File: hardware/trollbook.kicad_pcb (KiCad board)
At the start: 2 copper layers, 100 x 100 mm, 92 parts, among them P1 VGA, P10 CONN_1, P2 LCD, P3 SPI, P4 CONN_12, P5 CONN_2, P6 CONN_2, P7 CONN_2, P8 CONN_4, P9 CONN_2, U1 XC95288-208, U10 74LS574, U11 74LS574, U12 HY57V561620, U13 HY57V561620, U15 74HC4002, U16 ADA4851-4, U19 74HC139, U2 MC68030, U20 74HC10, U3 MC68882, U4 IDT71V416, U5 TLC7524, U6 74LS574, U7 39F040, U8 TLC7524, U9 74LS574, Y1 50 MHz, Y2 12.288 MHz

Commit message: fixed some erc/drc violations
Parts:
- added P11: CONN_2, PIN_ARRAY_2X1, F.Cu at (142.8, 153.7)
- P2: value LCD -> LCD_CONN
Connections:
- P2 pad GND: (no net) -> GND
- U1 pad 44: (no net) -> /EXTINT
- U15 pad 10: (no net) -> 3V3
- U15 pad 11: (no net) -> 3V3
- U15 pad 12: (no net) -> 3V3
- U15 pad 9: (no net) -> 3V3
- U19 pad 1: (no net) -> 3V3
- U19 pad 2: (no net) -> 3V3
- U19 pad 3: (no net) -> 3V3
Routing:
- net /EXTINT: track 0.00 -> 39.9 mm, vias 0 -> 4
- net 3V3: track 688.5 -> 704.6 mm
- net (no net): track 0.00 -> 4.55 mm, vias 0 -> 2
- net /CLK12: track 43.0 -> 42.2 mm
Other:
- board text added: "CPU"
- board text added: "DAC"
- board text added: "DRAM"
- board text added: "FPU"
- board text added: "GLUE"
- board text added: "ROM"
- board text added: "SRAM"

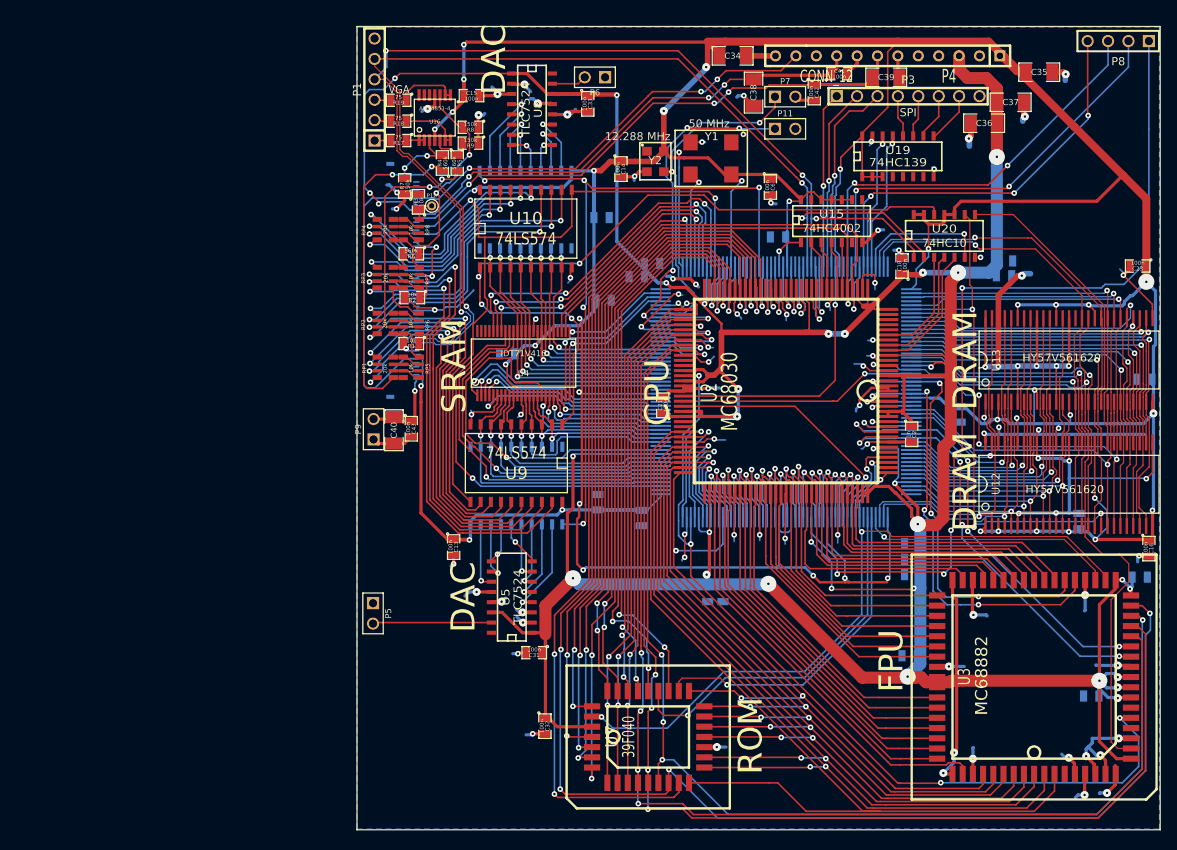
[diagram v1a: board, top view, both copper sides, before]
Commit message: ground plane stitching
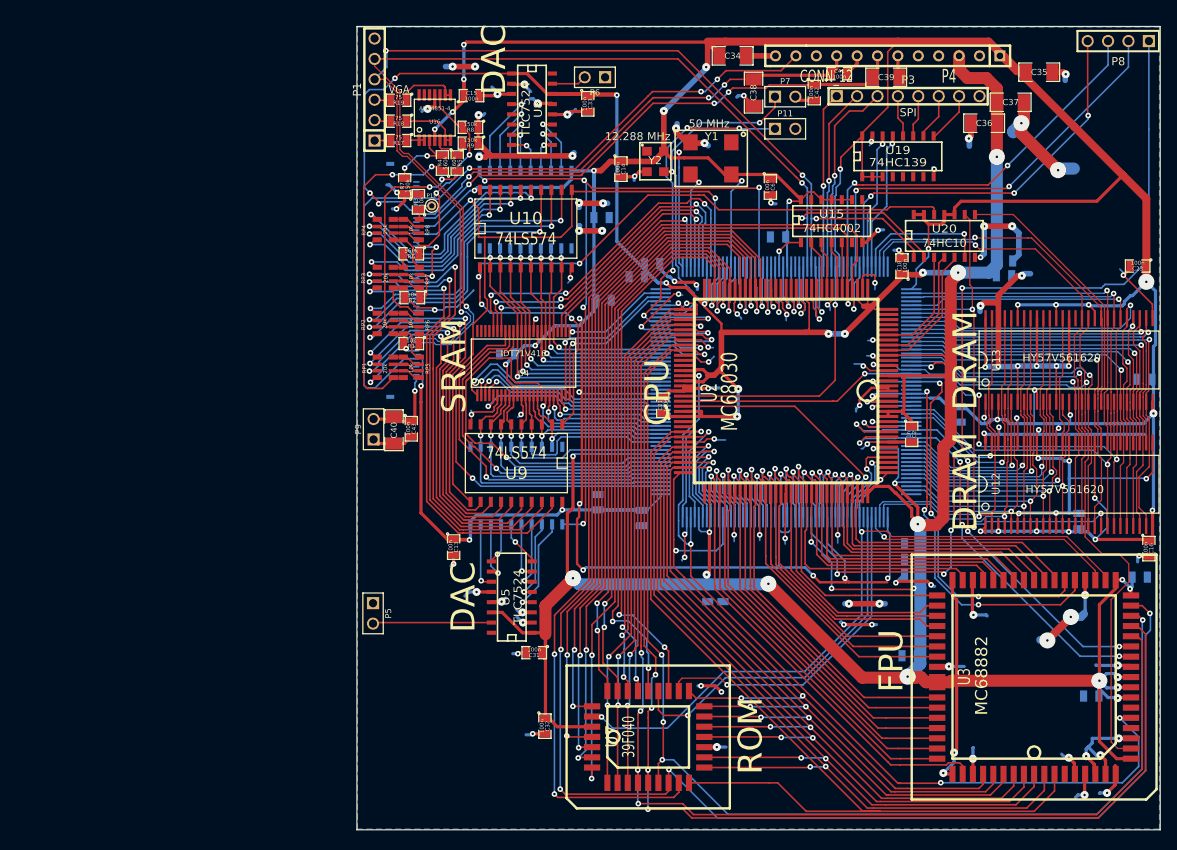
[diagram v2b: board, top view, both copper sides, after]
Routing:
- net GND: track 418.6 -> 484.4 mm, vias 85 -> 98
- net (no net): track 4.55 -> 24.7 mm, vias 2 -> 12
- net /DSACK1: track 54.8 -> 53.8 mm
- net /DSACK0: track 55.0 -> 53.9 mm
- net /D21: track 38.7 -> 39.4 mm

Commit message: arne
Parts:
- added R10: 10k, SM0805, F.Cu at (181.7, 146.7)
- added R11: 10k, SM0805, F.Cu at (183.8, 146.7)
- added R12: 10k, SM0805, F.Cu at (186.0, 146.7)
- added R13: 10k, SM0805, F.Cu at (188.2, 146.7)
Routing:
- net 3V3: track 704.6 -> 719.2 mm
- net N-0000055: track 49.9 -> 53.4 mm
- net N-0000056: track 51.6 -> 54.9 mm
- net N-0000057: track 53.0 -> 56.2 mm
- net N-0000058: track 110.4 -> 113.4 mm

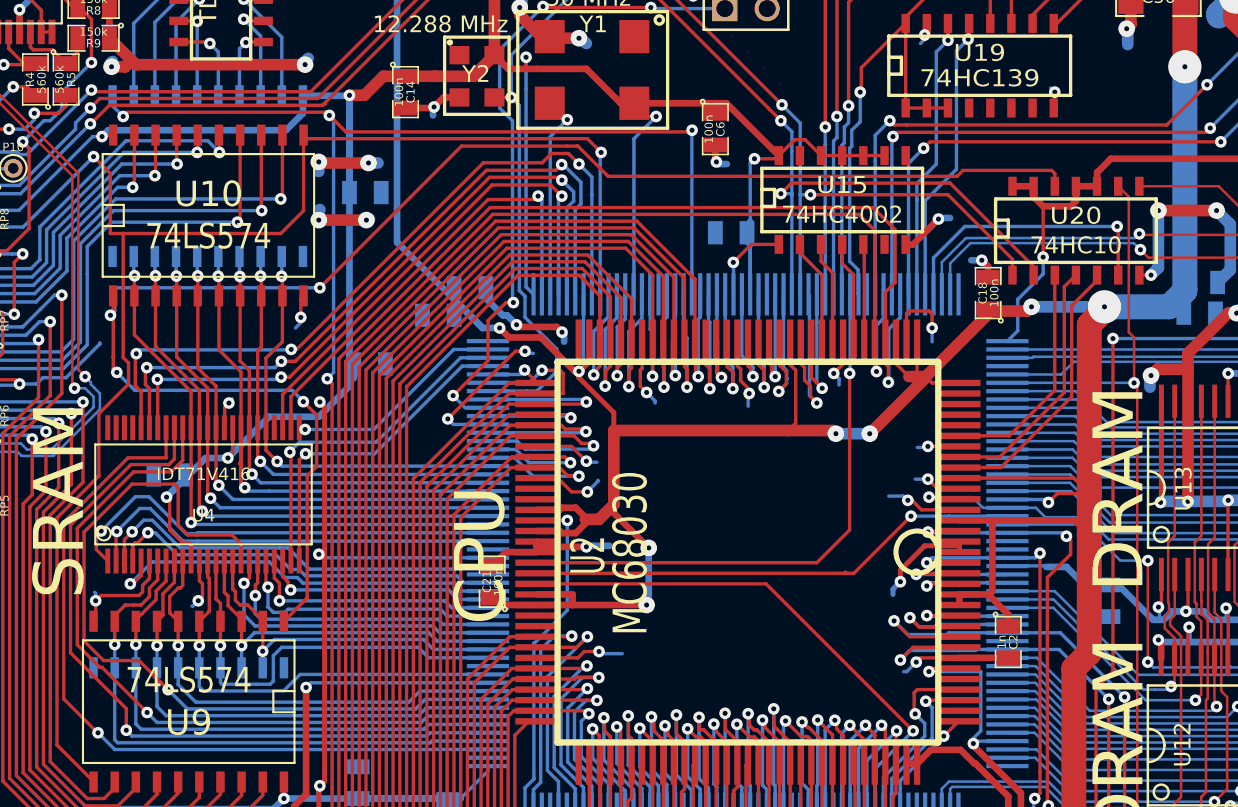
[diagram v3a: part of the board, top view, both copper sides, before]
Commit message: fixed a couple of voltage issues
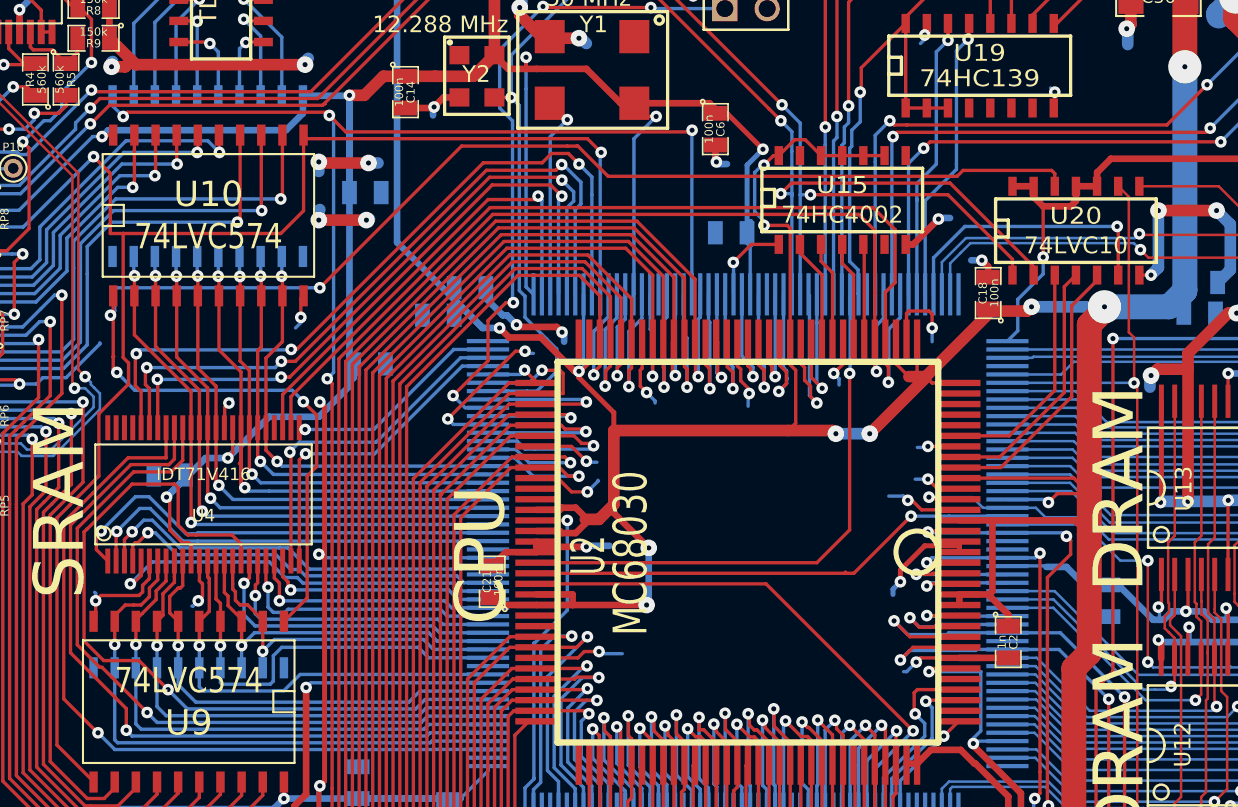
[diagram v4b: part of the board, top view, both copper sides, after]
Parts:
- U10, U11, U6, U9: value 74LS574 -> 74LVC574
- U20: value 74HC10 -> 74LVC10
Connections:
- U15 pad 10: 3V3 -> +5V
- U15 pad 11: 3V3 -> +5V
- U15 pad 12: 3V3 -> +5V
- U15 pad 14: 3V3 -> +5V
- U15 pad 9: 3V3 -> +5V
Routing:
- net +5V: track 609.3 -> 630.1 mm, vias 34 -> 36
- net 3V3: track 719.2 -> 706.0 mm
